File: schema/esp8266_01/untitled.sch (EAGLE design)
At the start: 24 parts, among them IC1 LD117AS33TR, J1 DCJ0202, Q1 BC857ASMD, X2 12 MHz

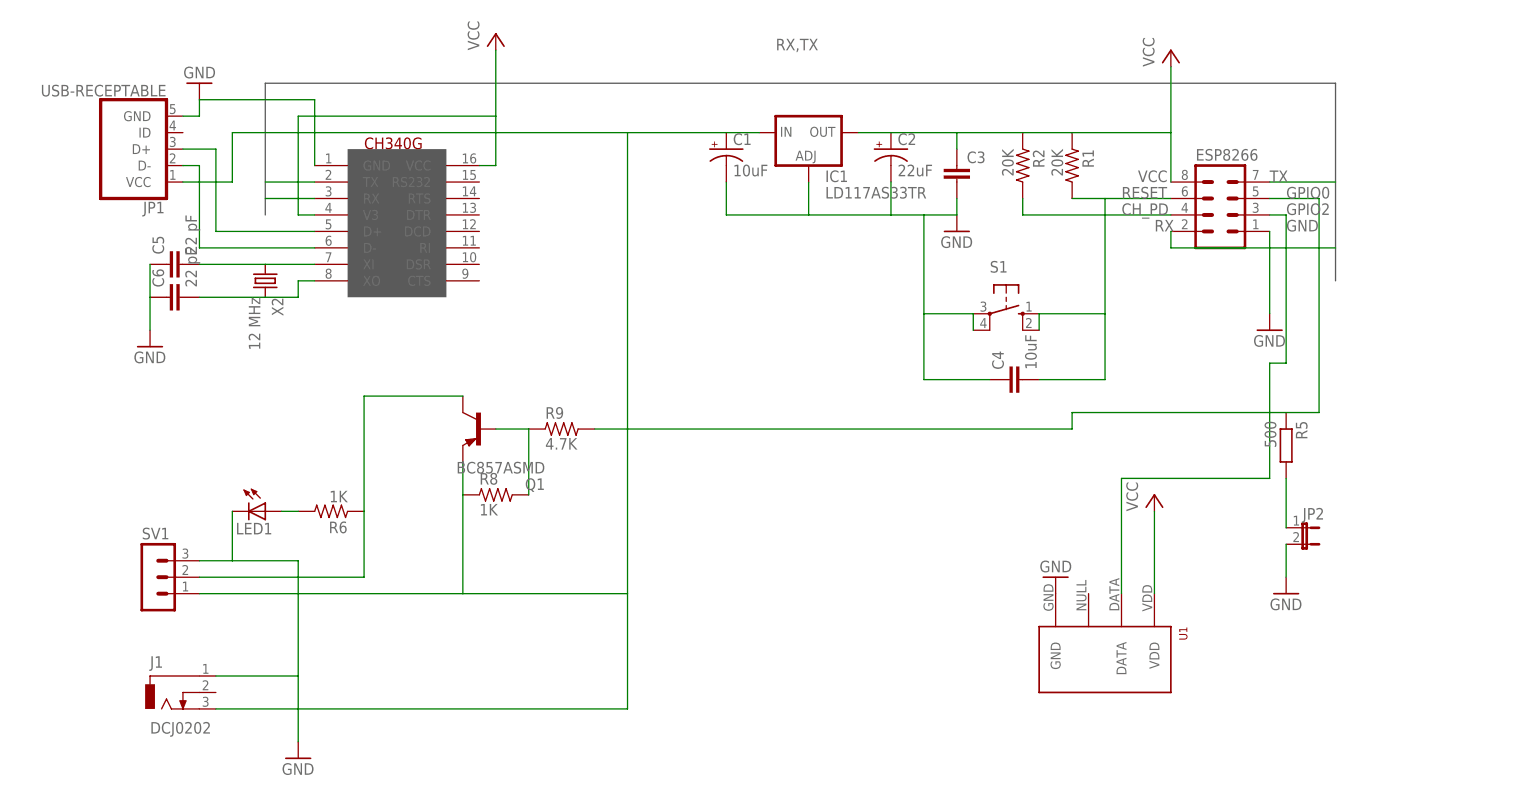
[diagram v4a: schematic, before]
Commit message: Fixed all schemas. Just needed to change miscro USB sockets
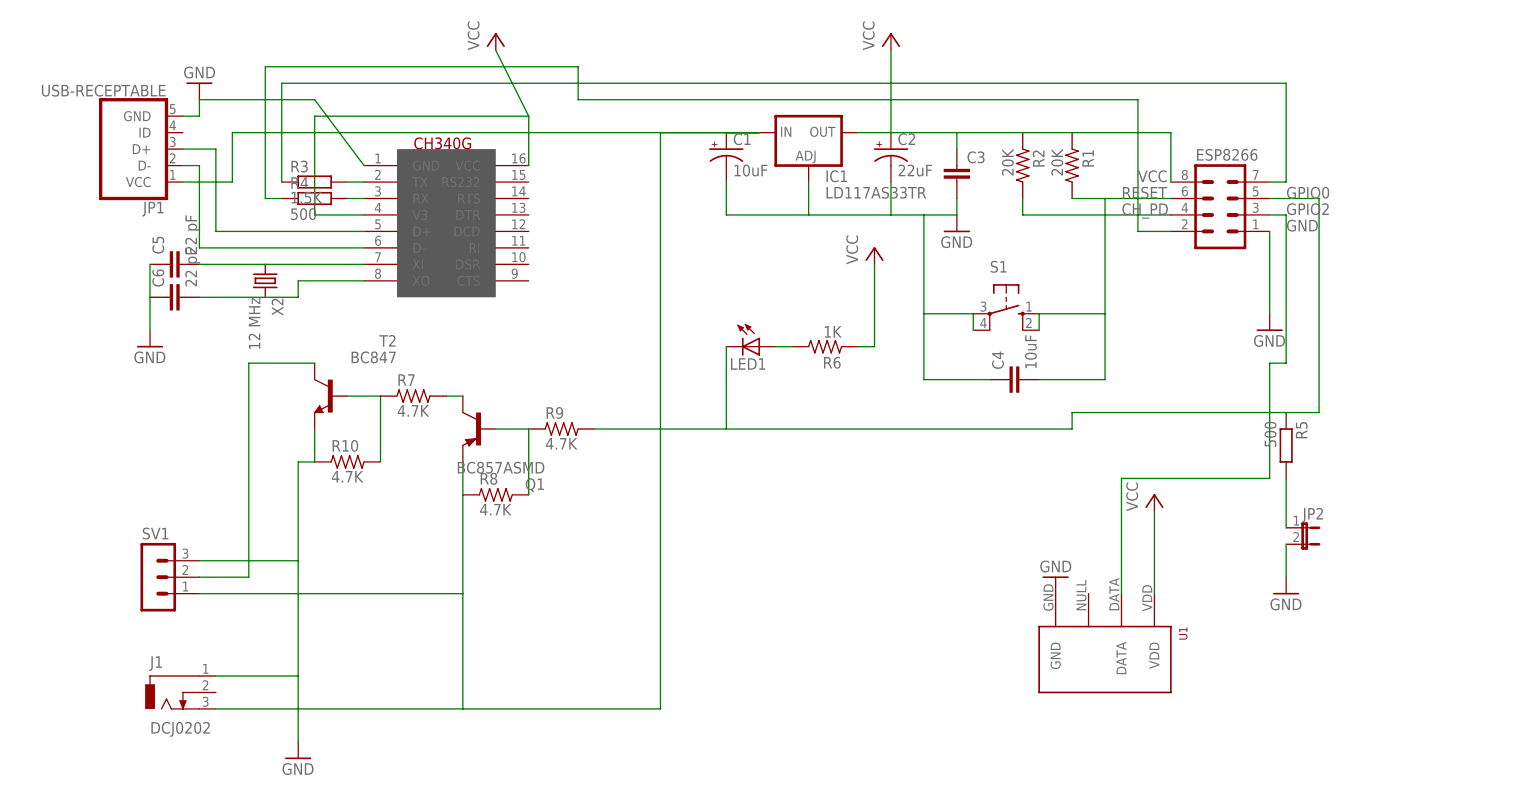
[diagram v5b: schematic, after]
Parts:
- added R10, R7: 4.7K, rc-master:R_0805
- added R3: 1.5K, resistor:R-EU_R0805
- added R4: 500, resistor:R-EU_R0805
- added T2: BC847, transistor:BC847
- R8: value 1K -> 4.7K
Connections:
- removed net RX: ESP8266.2, U$1.RX
- removed net TX: ESP8266.7, U$1.TX
- new net N$36: ESP8266.7, R3.1
- new net N$37: R3.2, U$1.TX
- new net N$40: ESP8266.2, R4.1
- new net N$41: R4.2, U$1.RX
- new net N$46: R10.2, R7.1, T2.B
- new net N$48: SV1.2, T2.C
- net GND: now also R10.1, T2.E; no longer LED1.C
- net GPIO0: now also LED1.C
- net N$7: now also R7.2; no longer R6.1, SV1.2
- net VCC: now also R6.1
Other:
- moved on the sheet: LED1, R6

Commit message: Finished ver 1.0 for both boards
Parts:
- C1: value 10uF -> 100nF
- C3: value (none) -> 10uF
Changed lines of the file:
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@@
 <part name="IC1" library="v-reg" deviceset="LD117A?*" device="S" technology="33TR"/>
 <part name="ESP8266" library="con-lstb" deviceset="MA04-2" device=""/>
-<part name="C1" library="rcl" deviceset="CPOL-US" device="E2-4" value="10uF"/>
+<part name="C1" library="rcl" deviceset="CPOL-US" device="E2-4" value="100nF"/>
 <part name="C2" library="rcl" deviceset="CPOL-US" device="E2-4" value="22uF"/>
 <part name="R1" library="rc-master" deviceset="R_" device="0805" value="20K"/>
@@
 <part name="R5" library="rcl" deviceset="R-EU_" device="0204/5" value="500"/>
 <part name="S1" library="switch-omron" deviceset="10-XX" device=""/>
-<part name="C3" library="rcl" deviceset="C-EU" device="C0805"/>
+<part name="C3" library="rcl" deviceset="C-EU" device="C0805" value="10uF"/>
 <part name="C4" library="capacitor-wima" deviceset="C" device="5/2.5" value="10uF"/>
 <part name="U1" library="RHT03_DHT-22_AM2302" deviceset="RHT03_DHT-22_AM2302" device=""/>
